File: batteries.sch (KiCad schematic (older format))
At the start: 6 parts

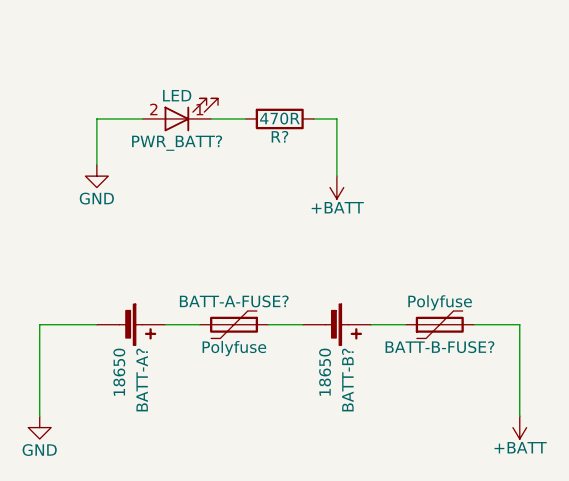
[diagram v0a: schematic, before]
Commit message: mpu6000 circuit complete + power circuit extracted + other changes
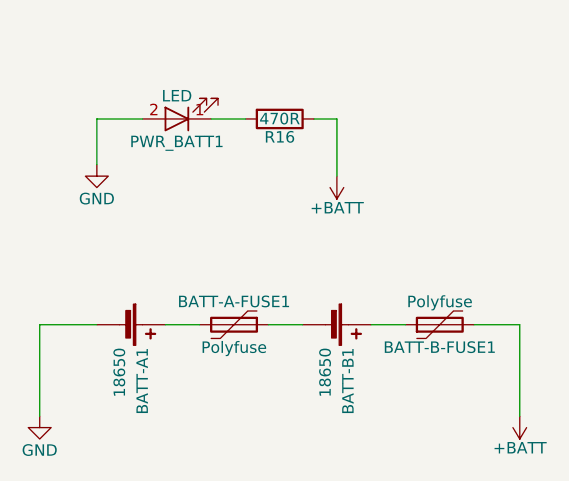
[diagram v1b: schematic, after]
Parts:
- gave numbers to parts that had none: 6
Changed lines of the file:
@@
 $Descr A4 11693 8268
 encoding utf-8
-Sheet 2 3
+Sheet 2 5
 Title "Batteries"
 Date ""
@@
 	4500 4050 4750 4050
 $Comp
-L Polyfuse BATT-B-FUSE?
+L Polyfuse BATT-B-FUSE1
 U 1 1 5B2CA0D4
 P 6250 4050
-F 0 "BATT-B-FUSE?" V 6150 4050 50  0000 C CNN
+F 0 "BATT-B-FUSE1" V 6150 4050 50  0000 C CNN
 F 1 "Polyfuse" V 6350 4050 50  0000 C CNN
 F 2 "" H 6300 3850 50  0001 L CNN
@@
 $EndComp
 $Comp
-L Polyfuse BATT-A-FUSE?
+L Polyfuse BATT-A-FUSE1
 U 1 1 5B2CA0DB
 P 5350 4050
-F 0 "BATT-A-FUSE?" V 5250 4050 50  0000 C CNN
+F 0 "BATT-A-FUSE1" V 5250 4050 50  0000 C CNN
 F 1 "Polyfuse" V 5450 4050 50  0000 C CNN
 F 2 "" H 5400 3850 50  0001 L CNN
@@
 	6600 4050 6600 4450
 $Comp
-L +BATT #PWR?
+L +BATT #PWR1228
 U 1 1 5B2CA0E3
 P 6600 4450
-F 0 "#PWR?" H 6600 4300 50  0001 C CNN
+F 0 "#PWR1228" H 6600 4300 50  0001 C CNN
 F 1 "+BATT" H 6600 4590 50  0000 C CNN
 F 2 "" H 6600 4450 50  0001 C CNN
@@
 	4500 4050 4500 4450
 $Comp
-L GND #PWR?
+L GND #PWR1225
 U 1 1 5B2CA0EA
 P 4500 4450
-F 0 "#PWR?" H 4500 4200 50  0001 C CNN
+F 0 "#PWR1225" H 4500 4200 50  0001 C CNN
 F 1 "GND" H 4500 4300 50  0000 C CNN
 F 2 "" H 4500 4450 50  0001 C CNN
@@
 $EndComp
 $Comp
-L Battery_Cell BATT-B?
+L Battery_Cell BATT-B1
 U 1 1 5B2CA0F0
 P 5750 4050
-F 0 "BATT-B?" H 5850 4150 50  0000 L CNN
+F 0 "BATT-B1" H 5850 4150 50  0000 L CNN
 F 1 "18650" H 5850 4050 50  0000 L CNN
 F 2 "Battery_Holders:Keystone_1042_1x18650" V 5750 4110 50  0001 C CNN
@@
 $EndComp
 $Comp
-L Battery_Cell BATT-A?
+L Battery_Cell BATT-A1
 U 1 1 5B2CA0F7
 P 4850 4050
-F 0 "BATT-A?" H 4950 4150 50  0000 L CNN
+F 0 "BATT-A1" H 4950 4150 50  0000 L CNN
 F 1 "18650" H 4950 4050 50  0000 L CNN
 F 2 "Battery_Holders:Keystone_1042_1x18650" V 4850 4110 50  0001 C CNN
@@
 	5250 3150 5400 3150
 $Comp
-L +BATT #PWR?
+L +BATT #PWR1227
 U 1 1 5B2CA103
 P 5800 3400
-F 0 "#PWR?" H 5800 3250 50  0001 C CNN
+F 0 "#PWR1227" H 5800 3250 50  0001 C CNN
 F 1 "+BATT" H 5800 3540 50  0000 C CNN
 F 2 "" H 5800 3400 50  0001 C CNN
@@
 $EndComp
 $Comp
-L LED PWR_BATT?
+L LED PWR_BATT1
 U 1 1 5B2CA109
 P 5100 3150
-F 0 "PWR_BATT?" H 5100 3250 50  0000 C CNN
+F 0 "PWR_BATT1" H 5100 3250 50  0000 C CNN
 F 1 "LED" H 5100 3050 50  0000 C CNN
 F 2 "LEDs:LED_0603" H 5100 3150 50  0001 C CNN
@@
 $EndComp
 $Comp
-L GND #PWR?
+L GND #PWR1226
 U 1 1 5B2CA110
 P 4750 3350
-F 0 "#PWR?" H 4750 3100 50  0001 C CNN
+F 0 "#PWR1226" H 4750 3100 50  0001 C CNN
 F 1 "GND" H 4750 3200 50  0000 C CNN
 F 2 "" H 4750 3350 50  0001 C CNN
@@
 $EndComp
 $Comp
-L R R?
+L R R16
 U 1 1 5B2CA116
 P 5550 3150
-F 0 "R?" V 5630 3150 50  0000 C CNN
+F 0 "R16" V 5630 3150 50  0000 C CNN
 F 1 "470R" V 5550 3150 50  0000 C CNN
 F 2 "Resistors_SMD:R_0603" V 5480 3150 50  0001 C CNN

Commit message: zone movement + routing of all circuits
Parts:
- BATT-A-FUSE1, BATT-B-FUSE1: footprint (none) -> Fuse:Fuse_1812_4532Metric
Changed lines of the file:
@@
 EESchema Schematic File Version 2
 LIBS:power
-LIBS:device
 LIBS:transistors
 LIBS:conn
@@
 LIBS:sensors
 LIBS:dc-dc
+LIBS:device
 LIBS:dc26-cache
 EELAYER 25 0
@@
 $Descr A4 11693 8268
 encoding utf-8
-Sheet 2 6
+Sheet 6 6
 Title "Batteries"
 Date ""
@@
 F 0 "BATT-B-FUSE1" V 6150 4050 50  0000 C CNN
 F 1 "Polyfuse" V 6350 4050 50  0000 C CNN
-F 2 "" H 6300 3850 50  0001 L CNN
+F 2 "Fuse:Fuse_1812_4532Metric" H 6300 3850 50  0001 L CNN
 F 3 "" H 6250 4050 50  0001 C CNN
 	1    6250 4050
@@
 F 0 "BATT-A-FUSE1" V 5250 4050 50  0000 C CNN
 F 1 "Polyfuse" V 5450 4050 50  0000 C CNN
-F 2 "" H 5400 3850 50  0001 L CNN
+F 2 "Fuse:Fuse_1812_4532Metric" H 5400 3850 50  0001 L CNN
 F 3 "" H 5350 4050 50  0001 C CNN
 	1    5350 4050
@@
 	6600 4050 6600 4450
 $Comp
-L +BATT #PWR1228
+L +BATT #PWR01246
 U 1 1 5B2CA0E3
 P 6600 4450
-F 0 "#PWR1228" H 6600 4300 50  0001 C CNN
+F 0 "#PWR01246" H 6600 4300 50  0001 C CNN
 F 1 "+BATT" H 6600 4590 50  0000 C CNN
 F 2 "" H 6600 4450 50  0001 C CNN
@@
 	4500 4050 4500 4450
 $Comp
-L GND #PWR1225
+L GND #PWR01247
 U 1 1 5B2CA0EA
 P 4500 4450
-F 0 "#PWR1225" H 4500 4200 50  0001 C CNN
+F 0 "#PWR01247" H 4500 4200 50  0001 C CNN
 F 1 "GND" H 4500 4300 50  0000 C CNN
 F 2 "" H 4500 4450 50  0001 C CNN
@@
 	5250 3150 5400 3150
 $Comp
-L +BATT #PWR1227
+L +BATT #PWR01248
 U 1 1 5B2CA103
 P 5800 3400
-F 0 "#PWR1227" H 5800 3250 50  0001 C CNN
+F 0 "#PWR01248" H 5800 3250 50  0001 C CNN
 F 1 "+BATT" H 5800 3540 50  0000 C CNN
 F 2 "" H 5800 3400 50  0001 C CNN
@@
 $EndComp
 $Comp
-L GND #PWR1226
+L GND #PWR01249
 U 1 1 5B2CA110
 P 4750 3350
-F 0 "#PWR1226" H 4750 3100 50  0001 C CNN
+F 0 "#PWR01249" H 4750 3100 50  0001 C CNN
 F 1 "GND" H 4750 3200 50  0000 C CNN
 F 2 "" H 4750 3350 50  0001 C CNN

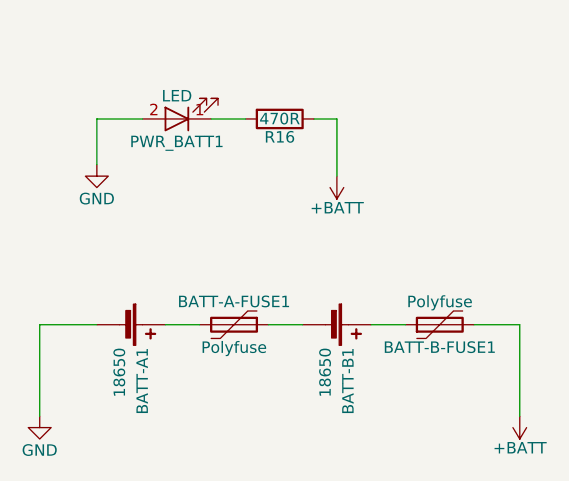
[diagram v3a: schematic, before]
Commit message: splitting led power out from 5v so that we can insert the mosfet
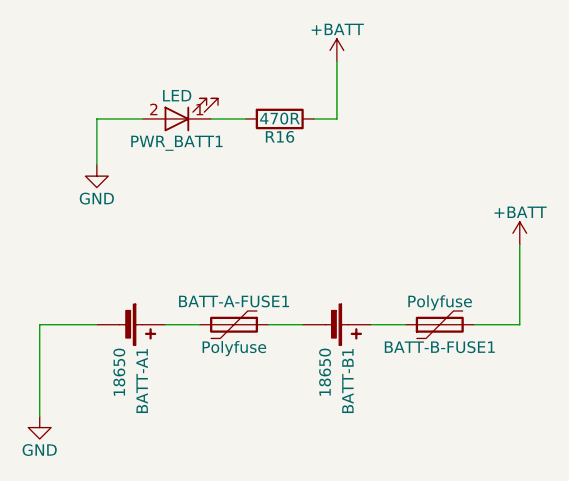
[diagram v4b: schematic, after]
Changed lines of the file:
@@
 	0    1    1    0
 $EndComp
-Wire Wire Line
-	6600 4050 6600 4450
 $Comp
-L +BATT #PWR01246
+L +BATT #PWR1246
 U 1 1 5B2CA0E3
-P 6600 4450
-F 0 "#PWR01246" H 6600 4300 50  0001 C CNN
-F 1 "+BATT" H 6600 4590 50  0000 C CNN
-F 2 "" H 6600 4450 50  0001 C CNN
-F 3 "" H 6600 4450 50  0001 C CNN
-	1    6600 4450
-	-1   0    0    1
+P 6600 3700
+F 0 "#PWR1246" H 6600 3550 50  0001 C CNN
+F 1 "+BATT" H 6600 3840 50  0000 C CNN
+F 2 "" H 6600 3700 50  0001 C CNN
+F 3 "" H 6600 3700 50  0001 C CNN
+	1    6600 3700
+	1    0    0    -1
 $EndComp
 Wire Wire Line
 	4500 4050 4500 4450
 $Comp
-L GND #PWR01247
+L GND #PWR1243
 U 1 1 5B2CA0EA
 P 4500 4450
-F 0 "#PWR01247" H 4500 4200 50  0001 C CNN
+F 0 "#PWR1243" H 4500 4200 50  0001 C CNN
 F 1 "GND" H 4500 4300 50  0000 C CNN
 F 2 "" H 4500 4450 50  0001 C CNN
@@
 	5700 3150 5800 3150
 Wire Wire Line
-	5800 3150 5800 3400
-Wire Wire Line
 	5250 3150 5400 3150
 $Comp
-L +BATT #PWR01248
+L +BATT #PWR1245
 U 1 1 5B2CA103
-P 5800 3400
-F 0 "#PWR01248" H 5800 3250 50  0001 C CNN
-F 1 "+BATT" H 5800 3540 50  0000 C CNN
-F 2 "" H 5800 3400 50  0001 C CNN
-F 3 "" H 5800 3400 50  0001 C CNN
-	1    5800 3400
-	-1   0    0    1
+P 5800 2900
+F 0 "#PWR1245" H 5800 2750 50  0001 C CNN
+F 1 "+BATT" H 5800 3040 50  0000 C CNN
+F 2 "" H 5800 2900 50  0001 C CNN
+F 3 "" H 5800 2900 50  0001 C CNN
+	1    5800 2900
+	1    0    0    -1
 $EndComp
 $Comp
@@
 $EndComp
 $Comp
-L GND #PWR01249
+L GND #PWR1244
 U 1 1 5B2CA110
 P 4750 3350
-F 0 "#PWR01249" H 4750 3100 50  0001 C CNN
+F 0 "#PWR1244" H 4750 3100 50  0001 C CNN
 F 1 "GND" H 4750 3200 50  0000 C CNN
 F 2 "" H 4750 3350 50  0001 C CNN
@@
 	0    1    1    0
 $EndComp
+Wire Wire Line
+	5800 3150 5800 2900
+Wire Wire Line
+	6600 4050 6600 3700
 $EndSCHEMATC
